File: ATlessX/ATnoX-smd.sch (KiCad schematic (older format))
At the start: 41 parts, among them J1 EXT_PWR_SW, J2 ATX, J3 AT, J4 PWR_LED, SW1 Power, U1 74LS74, U2 74LS14, U3 L7905, U4 74HCT4060, U5 74HCT73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

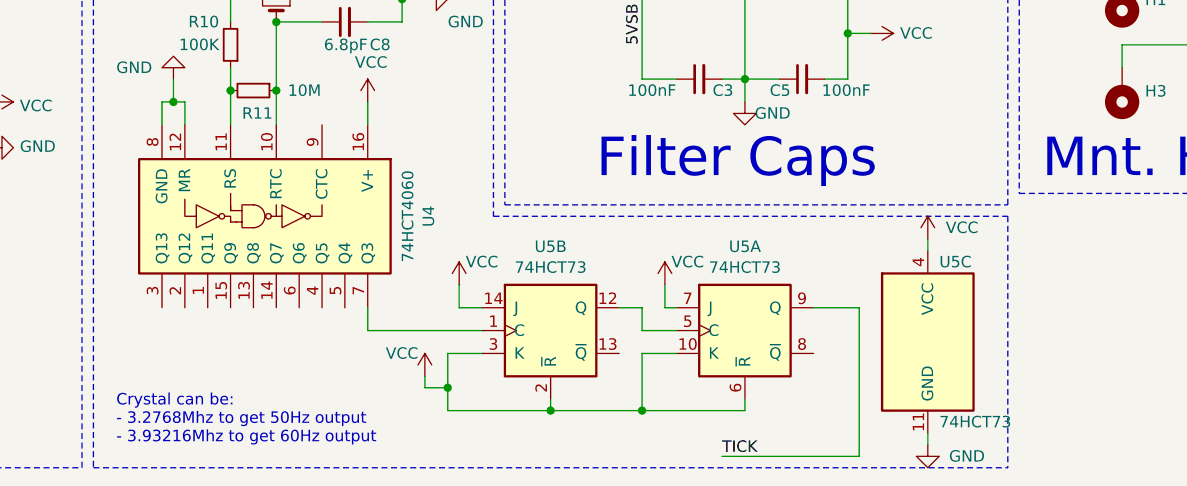
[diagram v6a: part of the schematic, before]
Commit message: Removed old versions, fix wrong pin connected to 4, rev 3.1
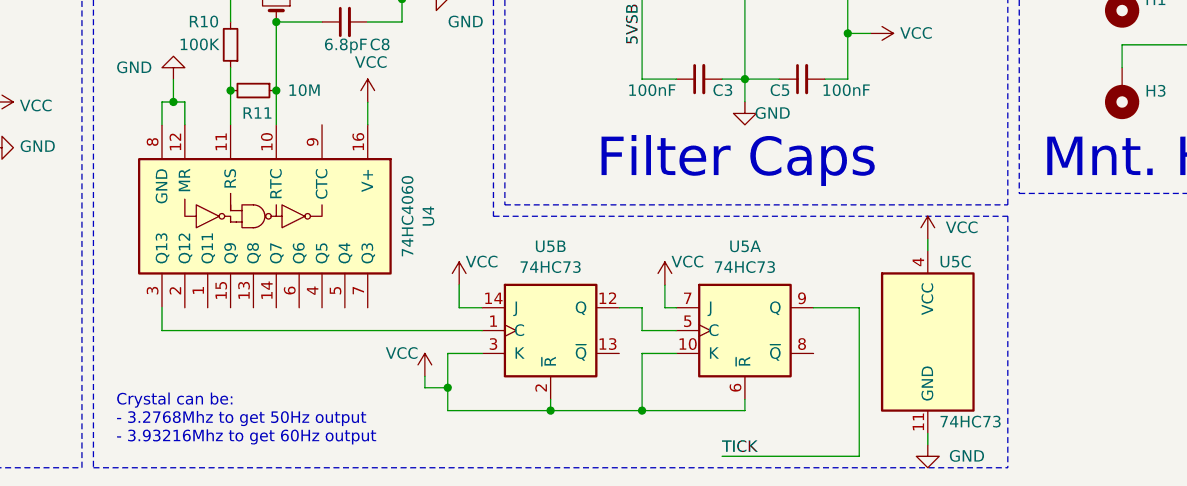
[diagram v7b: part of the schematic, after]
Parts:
- U4: value 74HCT4060 -> 74HC4060
- U5: value 74HCT73 -> 74HC73
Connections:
- net at U4.3 (Q13): now also U5.1 (C)
- net at U4.7 (Q3): no longer U5.1 (C)
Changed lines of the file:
@@
 	-1   0    0    1
-$EndComp
-$Comp
-L logic-4000:4060-SO U4
-U 1 1 5F5D971D
-P 3450 6600
-F 0 "U4" H 3450 7417 50  0000 C CNN
-F 1 "74HCT4060" H 3450 7326 50  0000 C CNN
-F 2 "Package_SO:SOIC-16_3.9x9.9mm_P1.27mm" H 3450 6050 50  0001 C CNN
-F 3 "https://www.onsemi.com/pub/Collateral/MC74HC4060A-D.PDF" H 3450 5950 60  0001 C CNN
-	1    3450 6600
-	0    1    1    0
 $EndComp
 Wire Wire Line
@@
 P 5650 7100
 F 0 "U5" H 5650 7467 50  0000 C CNN
-F 1 "74HCT73" H 5650 7376 50  0000 C CNN
+F 1 "74HC73" H 5650 7376 50  0000 C CNN
 F 2 "Package_SO:SOIC-14_3.9x8.7mm_P1.27mm" H 5650 7100 50  0001 C CNN
 F 3 "http://www.ti.com/lit/gpn/sn74LS73" H 5650 7100 50  0001 C CNN
@@
 P 4800 7100
 F 0 "U5" H 4800 7467 50  0000 C CNN
-F 1 "74HCT73" H 4800 7376 50  0000 C CNN
+F 1 "74HC73" H 4800 7376 50  0000 C CNN
 F 2 "Package_SO:SOIC-14_3.9x8.7mm_P1.27mm" H 4800 7100 50  0001 C CNN
 F 3 "http://www.ti.com/lit/gpn/sn74LS73" H 4800 7100 50  0001 C CNN
@@
 P 6450 7150
 F 0 "U5" H 6500 7500 50  0000 L CNN
-F 1 "74HCT73" H 6500 6800 50  0000 L CNN
+F 1 "74HC73" H 6500 6800 50  0000 L CNN
 F 2 "Package_SO:SOIC-14_3.9x8.7mm_P1.27mm" H 6450 7150 50  0001 C CNN
 F 3 "http://www.ti.com/lit/gpn/sn74LS73" H 6450 7150 50  0001 C CNN
@@
 	6450 6700 6450 6750
 Wire Wire Line
-	4000 7000 4000 7100
-Wire Wire Line
-	4000 7100 4500 7100
-Wire Wire Line
 	5200 7000 5200 7100
 Wire Wire Line
@@
 Text Label 5550 7650 0    50   ~ 0
 TICK
+$Comp
+L logic-4000:4060-SO U4
+U 1 1 5F5D971D
+P 3450 6600
+F 0 "U4" H 3450 7417 50  0000 C CNN
+F 1 "74HC4060" H 3450 7326 50  0000 C CNN
+F 2 "Package_SO:SOIC-16_3.9x9.9mm_P1.27mm" H 3450 6050 50  0001 C CNN
+F 3 "https://www.onsemi.com/pub/Collateral/MC74HC4060A-D.PDF" H 3450 5950 60  0001 C CNN
+	1    3450 6600
+	0    1    1    0
+$EndComp
+Wire Wire Line
+	3100 7000 3100 7100
+Wire Wire Line
+	3100 7100 4500 7100
 $EndSCHEMATC
